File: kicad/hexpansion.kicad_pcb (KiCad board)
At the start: 2 copper layers, 16.5 x 36.6 mm, 11 parts, among them J1 Hexpansion-Connector, J2 SD Card breakout, U1 AT24CS32-SSHM

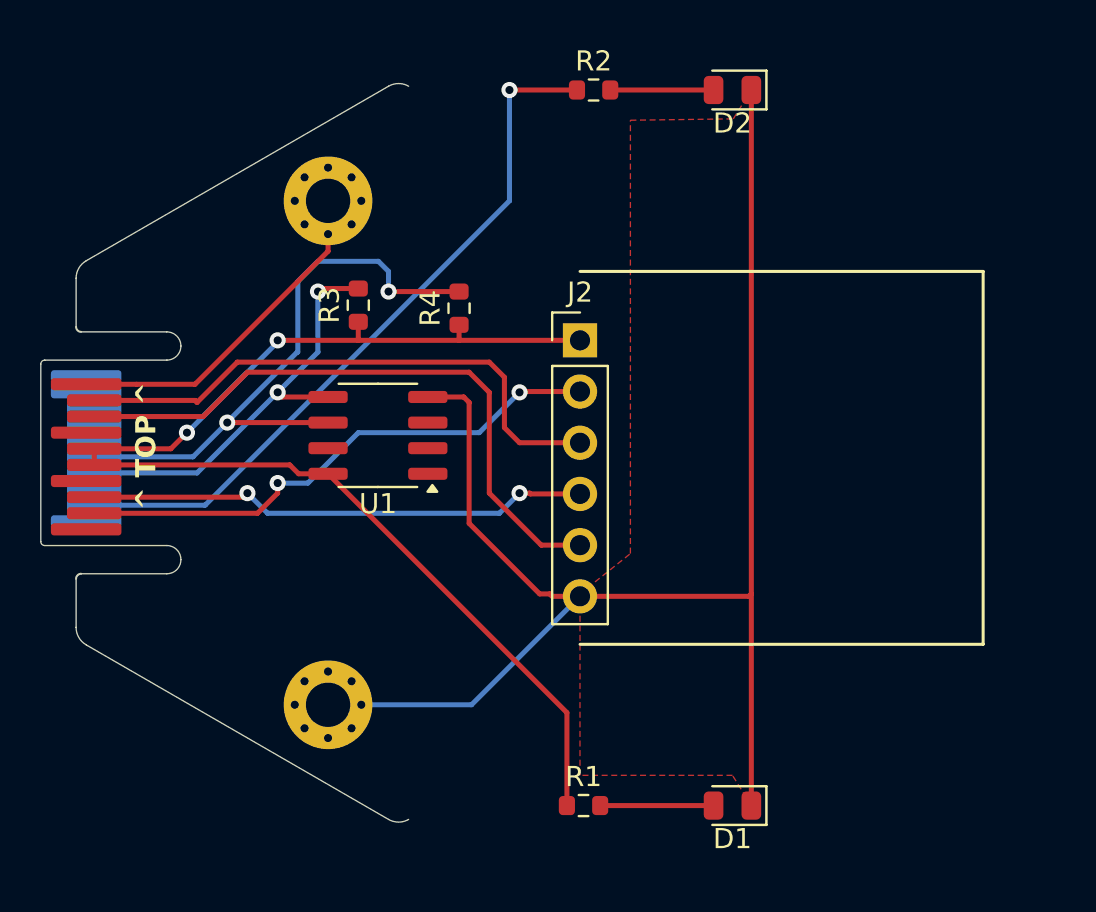
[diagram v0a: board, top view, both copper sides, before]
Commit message: Simplify
Based on the guidelines on r/PrintedCircuitBoards I'd removed most of the
use of nets in the schematic, and added ground fills on the PCB
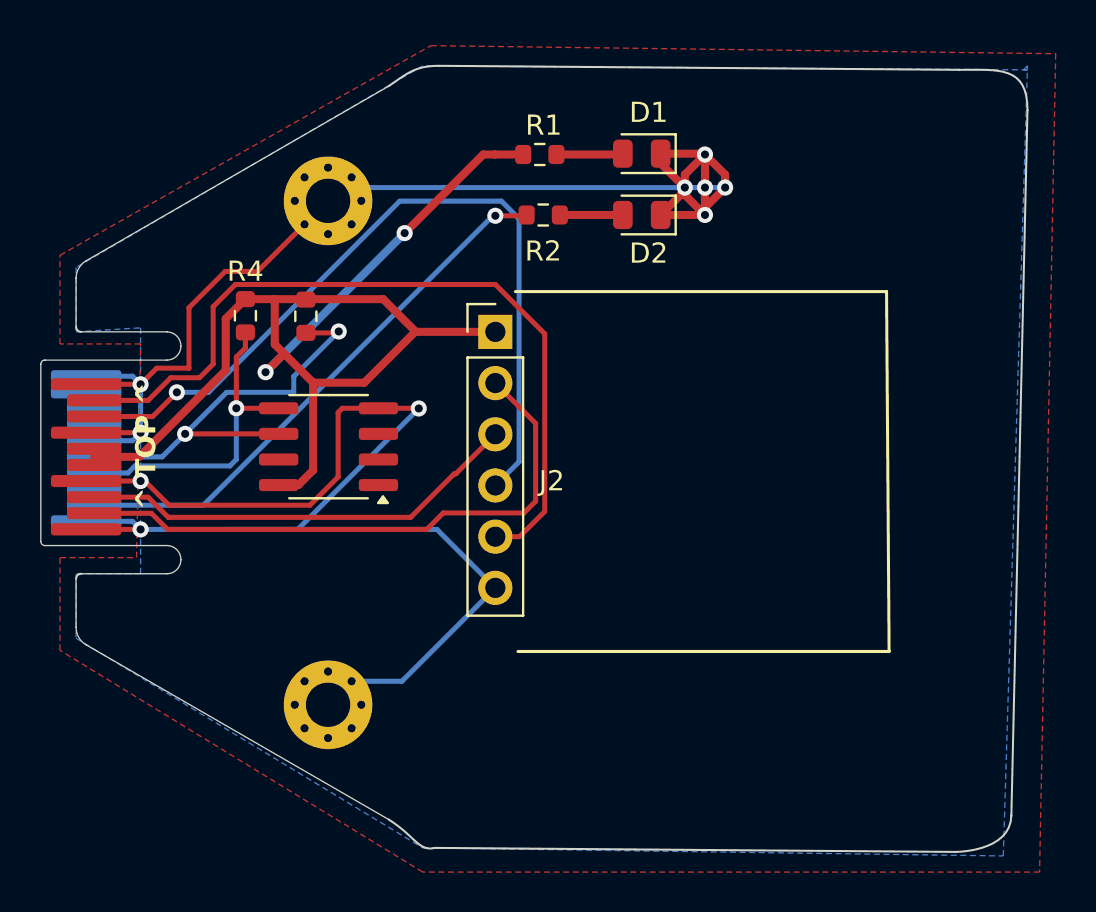
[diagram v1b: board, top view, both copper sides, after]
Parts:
- U1: value AT24CS32-SSHM -> AT24CS32
- moved D1 32.7 mm to (128.1, 85.2)
- moved R1 32.4 mm to (123.0, 85.2)
- moved R4 10.6 mm to (108.4, 93.2), turned to -90 degrees
- moved D2 7.66 mm to (128.1, 88.2)
- moved R2 6.69 mm to (123.2, 88.2)
- moved J2 4.22 mm to (120.8, 94.0)
- moved R3 2.66 mm to (111.4, 93.2), turned to -90 degrees
- moved U1 2.51 mm to (112.5, 99.7)
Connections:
- net CS renamed Net-(J1-HS_I)
- net Mounted renamed Net-(J1-LS_A)
- J1 pad 12: MOSI -> Net-(J1-HS_F)
- J1 pad 13: MISO -> Net-(J1-HS_G)
- J1 pad 18: CLK -> Net-(J1-HS_H)
- J1 pad 4: SDA -> Net-(J1-SDA)
- J1 pad 5: SCL -> Net-(J1-SCL)
- J2 pad 3: MOSI -> Net-(J1-HS_H)
- J2 pad 4: CLK -> Net-(J1-HS_G)
- J2 pad 5: MISO -> Net-(J1-HS_F)
- R3 pad 2: SDA -> Net-(J1-SCL)
- R4 pad 2: SCL -> Net-(J1-SDA)
- U1 pad 5: SDA -> Net-(J1-SDA)
- U1 pad 6: SCL -> Net-(J1-SCL)
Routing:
- net GND: track 91.2 -> 136.4 mm, vias 0 -> 10
- net Net-(J1-HS_G): track 0.00 -> 39.6 mm, vias 0 -> 1
- net Net-(J1-HS_F): track 0.00 -> 39.2 mm
- net MISO: track 31.5 -> 0.00 mm
- net SCL: track 30.4 -> 0.00 mm, vias 2 -> 0
- net MOSI: track 28.1 -> 0.00 mm
- net CLK: track 25.0 -> 0.00 mm, vias 2 -> 0
- net Net-(J1-HS_H): track 0.00 -> 22.0 mm
- net Net-(J1-SCL): track 0.00 -> 21.5 mm, vias 0 -> 2
- net SDA: track 21.2 -> 0.00 mm, vias 2 -> 0
- net Net-(J1-SDA): track 0.00 -> 15.9 mm, vias 0 -> 1
- net Net-(J1-LS_A): track 35.7 -> 27.4 mm
- net Net-(J1-HS_I): track 26.9 -> 29.5 mm, vias 2 -> 0
- net Net-(D1-A): track 5.62 -> 3.31 mm
- net Net-(D2-A): track 5.12 -> 3.12 mm
- added copper zone on B.Cu, net GND
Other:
- board size 16.5 x 36.6 mm -> 47.2 x 39 mm

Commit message: Add decoupling cap
Not yet sure if I'll need it, but definitely no harm in leaving room for
a decoupling cap for the flash chip.

The SD card breakout boards already have them built in.
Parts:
- added C1: C, Capacitor_SMD:C_0603_1608Metric_Pad1.08x0.95mm_HandSolder, F.Cu at (107.6, 101.5)
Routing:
- net 3.3: track 62.3 -> 65.1 mm
- net GND: vias 10 -> 17

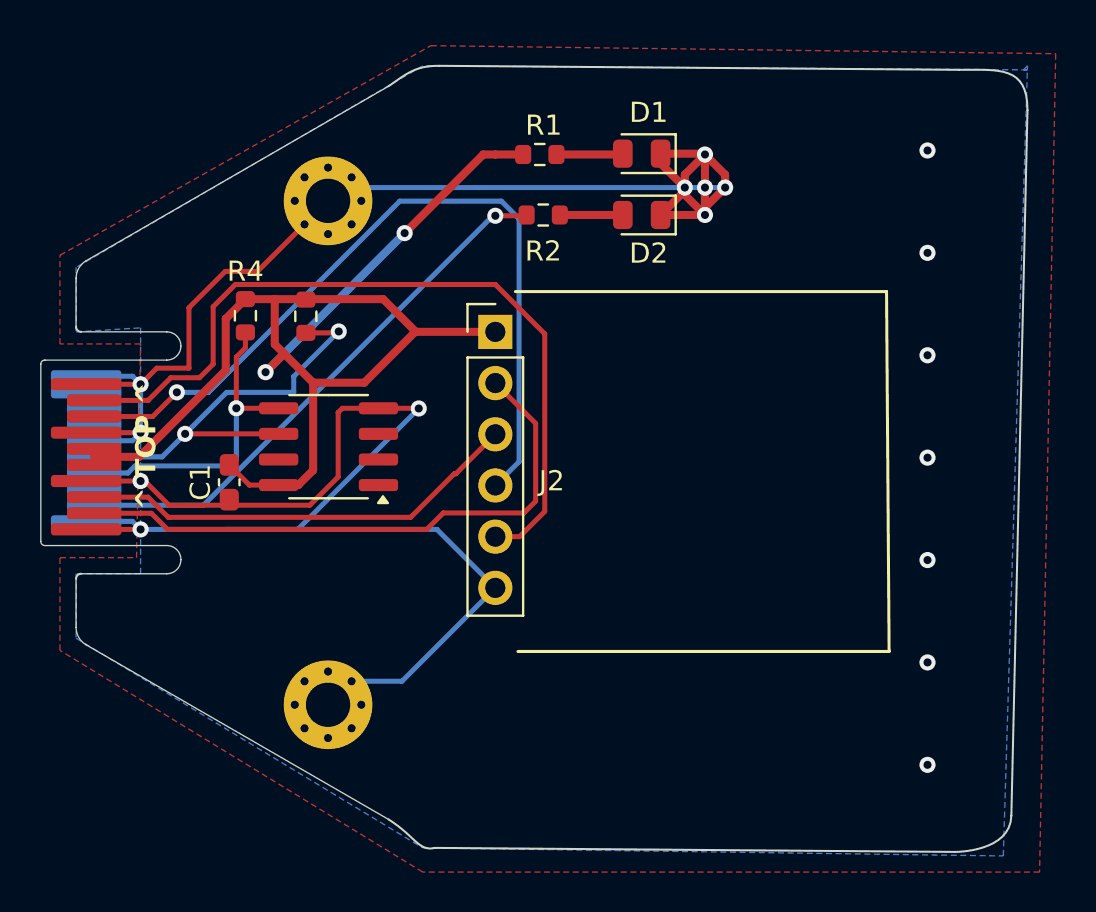
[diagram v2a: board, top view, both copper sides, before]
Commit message: Reorder GPIOs to simplify layout
Reordering the highspeed GPIOs made the SPI routing dead simple.
Reworked the rest of the board around that.
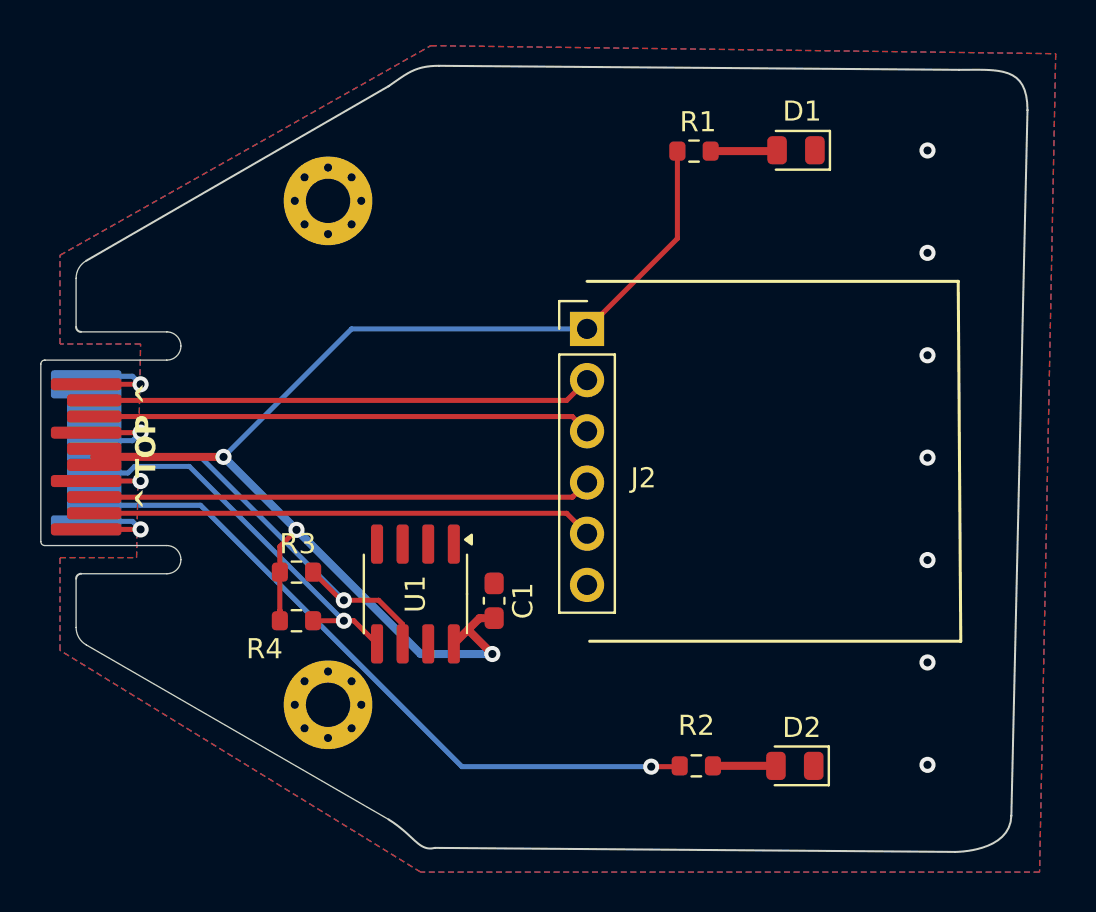
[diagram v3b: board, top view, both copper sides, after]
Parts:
- moved D2 28.4 mm to (135.7, 115.5)
- moved R2 28.4 mm to (130.8, 115.5)
- moved R4 15.3 mm to (110.9, 108.3), turned to 0 degrees
- moved C1 14.4 mm to (120.7, 107.3), turned to -90 degrees
- moved R3 12.7 mm to (110.9, 105.9), turned to 0 degrees
- moved U1 8.49 mm to (116.8, 107.0), turned to -90 degrees
- moved R1 7.65 mm to (130.7, 85.0)
- moved D1 7.65 mm to (135.7, 85.0)
- moved J2 4.55 mm to (125.3, 93.9)
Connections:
- J2 pad 2: Net-(J1-HS_I) -> Net-(J1-HS_F)
- J2 pad 3: Net-(J1-HS_H) -> Net-(J1-HS_G)
- J2 pad 4: Net-(J1-HS_G) -> Net-(J1-HS_H)
- J2 pad 5: Net-(J1-HS_F) -> Net-(J1-HS_I)
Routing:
- net GND: track 136.4 -> 20.6 mm, vias 17 -> 11
- net Net-(J1-HS_G): track 39.6 -> 24.8 mm, vias 1 -> 0
- net Net-(J1-HS_F): track 39.2 -> 24.9 mm
- net Net-(J1-LS_A): track 27.4 -> 34.6 mm
- net Net-(J1-HS_I): track 29.5 -> 24.9 mm
- net Net-(J1-SDA): track 15.9 -> 19.3 mm
- net Net-(J1-HS_H): track 22.0 -> 24.8 mm
- net Net-(J1-SCL): track 21.5 -> 21.8 mm, vias 2 -> 1
- net 3.3: vias 2 -> 3

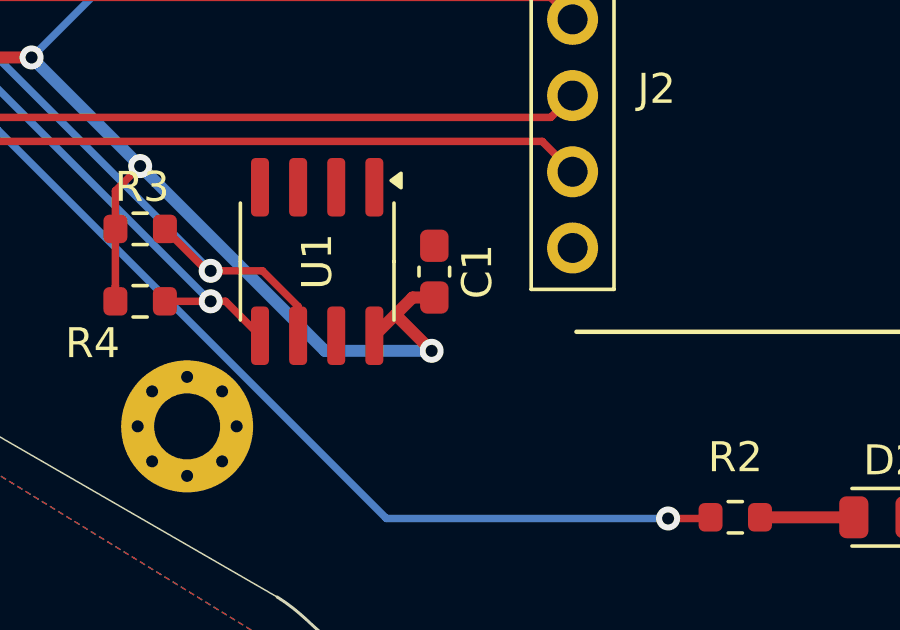
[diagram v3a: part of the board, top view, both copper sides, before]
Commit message: Tweak capacitor placement
Give the flash chip a touch more breathing room
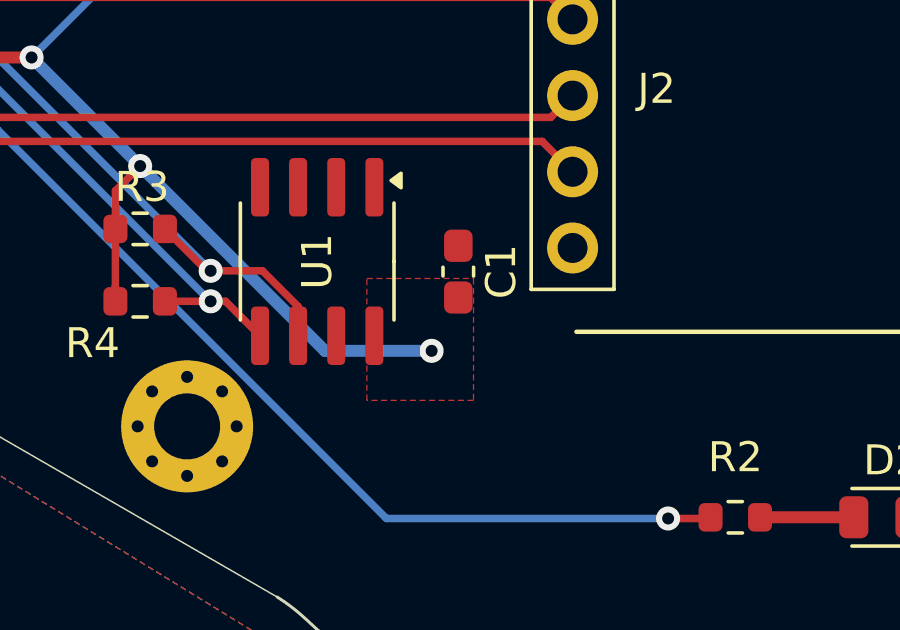
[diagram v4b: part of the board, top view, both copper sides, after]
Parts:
- moved C1 0.80 mm to (121.5, 107.3)
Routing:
- net 3.3: track 65.1 -> 60.8 mm
- added copper zone on F.Cu, net 3.3
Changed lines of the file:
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@@
 	(footprint "Capacitor_SMD:C_0603_1608Metric_Pad1.08x0.95mm_HandSolder"
 		(layer "F.Cu")
-		(at 120.74 107.3415 -90)
+		(at 121.539 107.3415 -90)
 		(descr "Capacitor SMD 0603 (1608 Metric), square (rectangular) end terminal, IPC-7351 nominal with elongated pad for handsoldering. (Body size source: IPC-SM-782 page 76, https://www.pcb-3d.com/wordpress/wp-content/uploads/ipc-sm-782a_amendment_1_and_2.pdf), generated with kicad-footprint-generator")
 		(tags "capacitor handsolder")
@@
 	)
 	(segment
-		(start 119.507 108.712)
-		(end 119.507 108.839)
-		(width 0.4)
-		(layer "F.Cu")
-		(net 5)
-	)
-	(segment
-		(start 120.74 108.204)
-		(end 120.015 108.204)
-		(width 0.4)
-		(layer "F.Cu")
-		(net 5)
-	)
-	(segment
 		(start 103.003 100.203)
 		(end 107.315 100.203)
@@
 	)
 	(segment
-		(start 119.507 108.712)
-		(end 118.74 109.479)
-		(width 0.4)
-		(layer "F.Cu")
-		(net 5)
-	)
-	(segment
-		(start 119.507 108.839)
-		(end 120.65 109.982)
-		(width 0.4)
-		(layer "F.Cu")
-		(net 5)
-	)
-	(segment
 		(start 129.832 89.37)
 		(end 125.349 93.853)
@@
 		(end 110.109 107.823)
 		(width 0.25)
-		(layer "F.Cu")
-		(net 5)
-	)
-	(segment
-		(start 120.015 108.204)
-		(end 119.507 108.712)
-		(width 0.4)
 		(layer "F.Cu")
 		(net 5)
@@
 	)
 	(zone
+		(net 5)
+		(net_name "3.3")
+		(layer "F.Cu")
+		(hatch edge 0.5)
+		(priority 1)
+		(connect_pads
+			(clearance 0.5)
+		)
+		(min_thickness 0.25)
+		(filled_areas_thickness no)
+		(fill yes
+			(thermal_gap 0.5)
+			(thermal_bridge_width 0.5)
+			(island_removal_mode 1)
+			(island_area_min 10)
+		)
+		(polygon
+			(pts
+				(xy 122.047 107.569) (xy 122.047 111.633) (xy 118.491 111.633) (xy 118.491 107.569)
+			)
+		)
+	)
+	(zone

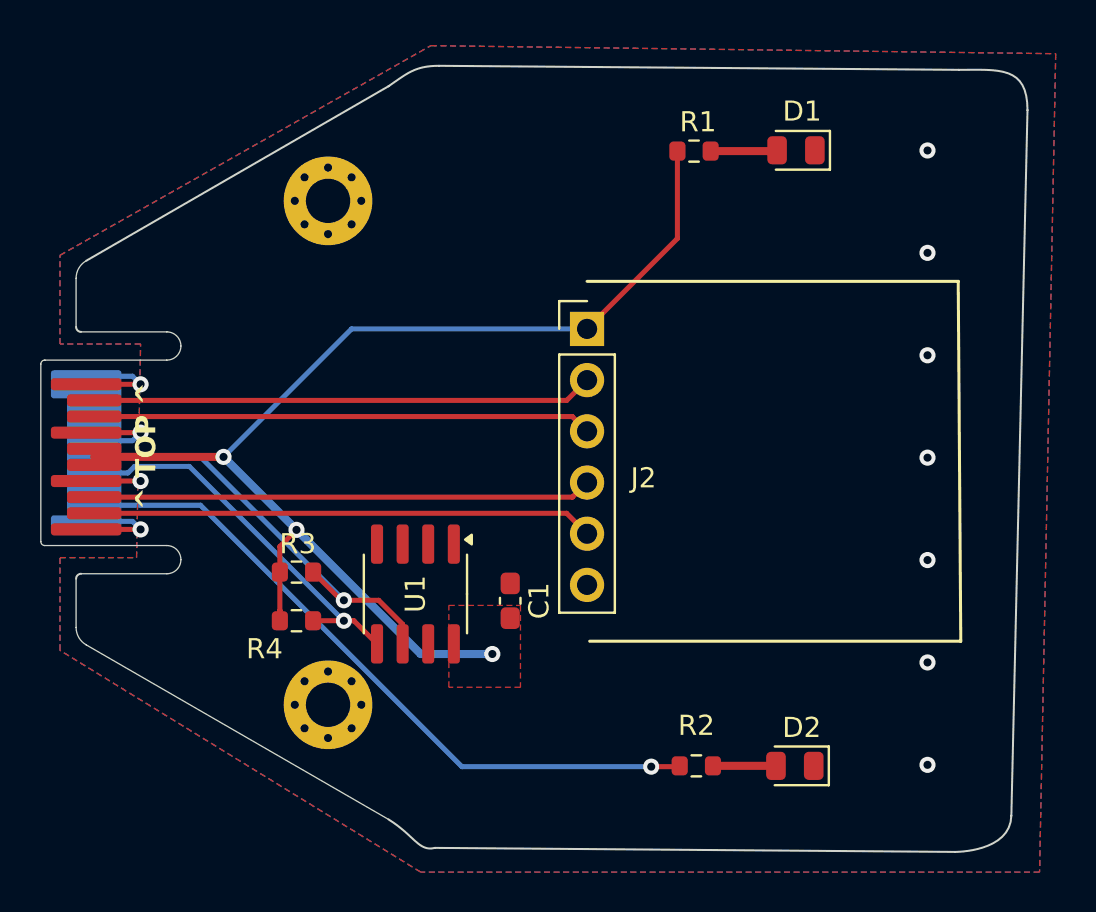
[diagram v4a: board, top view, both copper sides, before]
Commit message: Minor tweaks
* Move track away from mounting hole
* Tweak outline to fit within the limits - it was bulging over
  fractionally
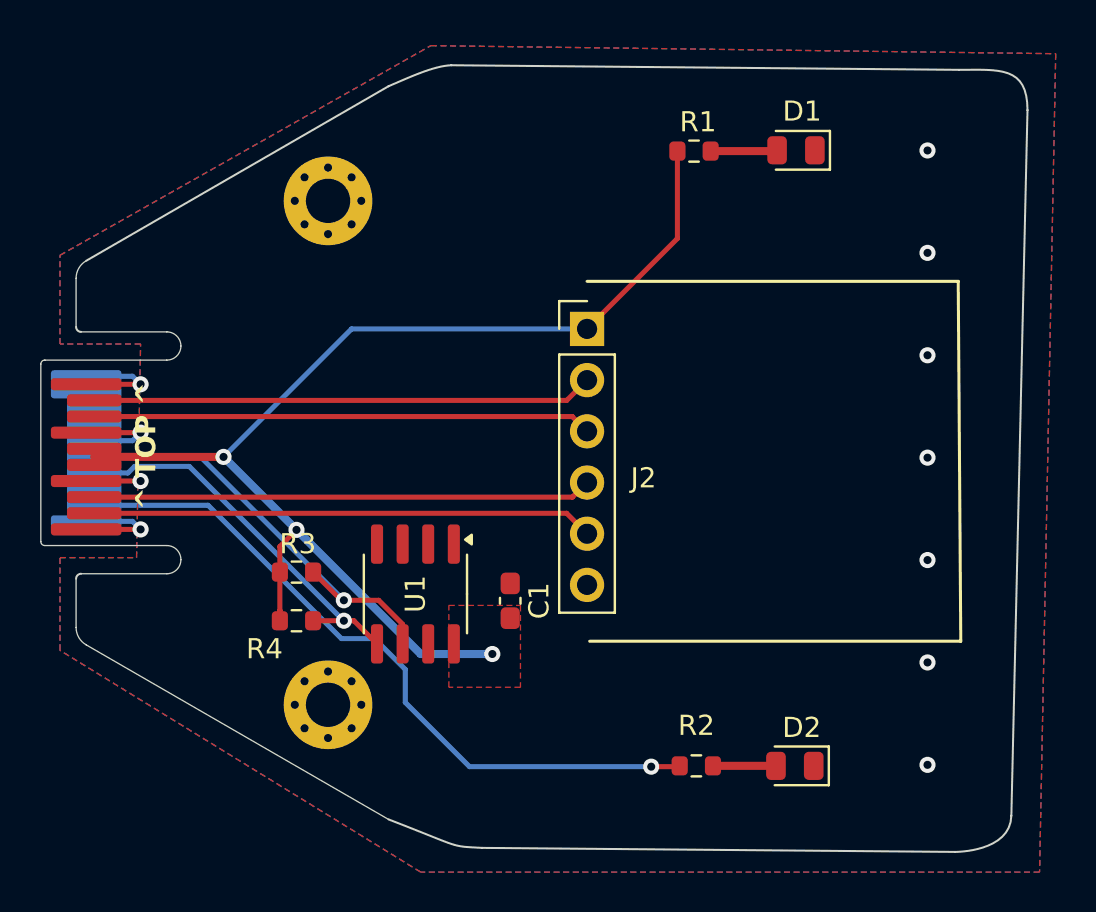
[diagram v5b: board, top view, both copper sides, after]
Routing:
- net Net-(J1-LS_A): track 34.6 -> 35.5 mm
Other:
- outline, holes or cut-outs redrawn
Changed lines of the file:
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@@
 	)
 	(gr_line
-		(start 117.8 119.6)
+		(start 120.142 119.6)
 		(end 143.6 119.8)
 		(stroke
@@
 	)
 	(gr_line
-		(start 118 80.8)
+		(start 118.618 80.772)
 		(end 143.8 81)
 		(stroke
@@
 	(gr_curve
 		(pts
-			(xy 115.499995 118.186522) (xy 116.8 119) (xy 117 119.8) (xy 117.8 119.6)
+			(xy 115.499995 118.186522) (xy 119.253 119.634) (xy 118.491 119.507) (xy 120.142 119.6)
 		)
 		(stroke
@@
 	(gr_curve
 		(pts
-			(xy 115.499995 81.813472) (xy 116.4 81.2) (xy 116.8 80.8) (xy 118 80.8)
+			(xy 115.499995 81.813472) (xy 116.459 81.407) (xy 117.729 80.8) (xy 118.618 80.772)
 		)
 		(stroke
@@
 	)
 	(segment
-		(start 119.142304 115.57)
-		(end 106.172304 102.6)
-		(width 0.25)
-		(layer "B.Cu")
-		(net 17)
-	)
-	(segment
-		(start 106.172304 102.6)
-		(end 100.9 102.6)
-		(width 0.25)
-		(layer "B.Cu")
-		(net 17)
-	)
-	(segment
-		(start 128.533 115.57)
-		(end 119.142304 115.57)
+		(start 119.515 115.57)
+		(end 128.533 115.57)
+		(width 0.25)
+		(layer "B.Cu")
+		(net 17)
+	)
+	(segment
+		(start 100.9 102.6)
+		(end 106.545 102.6)
+		(width 0.25)
+		(layer "B.Cu")
+		(net 17)
+	)
+	(segment
+		(start 106.545 102.6)
+		(end 113.161 109.216)
+		(width 0.25)
+		(layer "B.Cu")
+		(net 17)
+	)
+	(segment
+		(start 116.332 112.387)
+		(end 119.515 115.57)
+		(width 0.25)
+		(layer "B.Cu")
+		(net 17)
+	)
+	(segment
+		(start 113.161 109.216)
+		(end 114.804 109.216)
+		(width 0.25)
+		(layer "B.Cu")
+		(net 17)
+	)
+	(segment
+		(start 116.332 110.744)
+		(end 116.332 112.387)
+		(width 0.25)
+		(layer "B.Cu")
+		(net 17)
+	)
+	(segment
+		(start 114.804 109.216)
+		(end 116.332 110.744)
 		(width 0.25)
 		(layer "B.Cu")
@@
 		(min_thickness 0.25)
 		(filled_areas_thickness no)
-		(fill yes
+		(fill
 			(thermal_gap 0.5)
 			(thermal_bridge_width 0.5)
@@
 		(min_thickness 0.25)
 		(filled_areas_thickness no)
-		(fill yes
+		(fill
 			(thermal_gap 0.5)
 			(thermal_bridge_width 0.5)
